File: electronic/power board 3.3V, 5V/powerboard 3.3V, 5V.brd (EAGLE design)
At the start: 46.7 x 31.7 mm, 10 parts, among them IC1_5V REG1117, IC2_3.3V REG1117, X1 GND, X3_5V 5V, X4_3.3V 3.3V, X5 IN

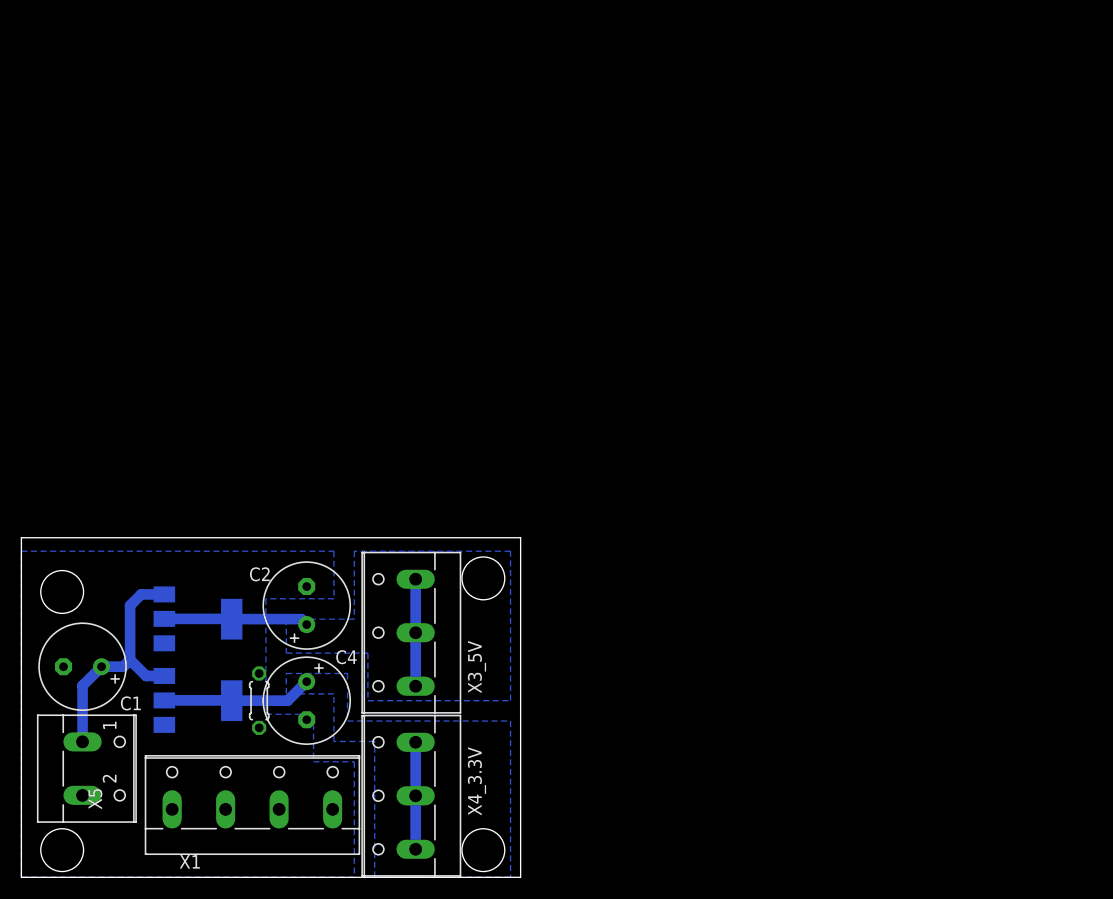
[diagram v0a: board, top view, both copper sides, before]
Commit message: moved schematics to the KiCad
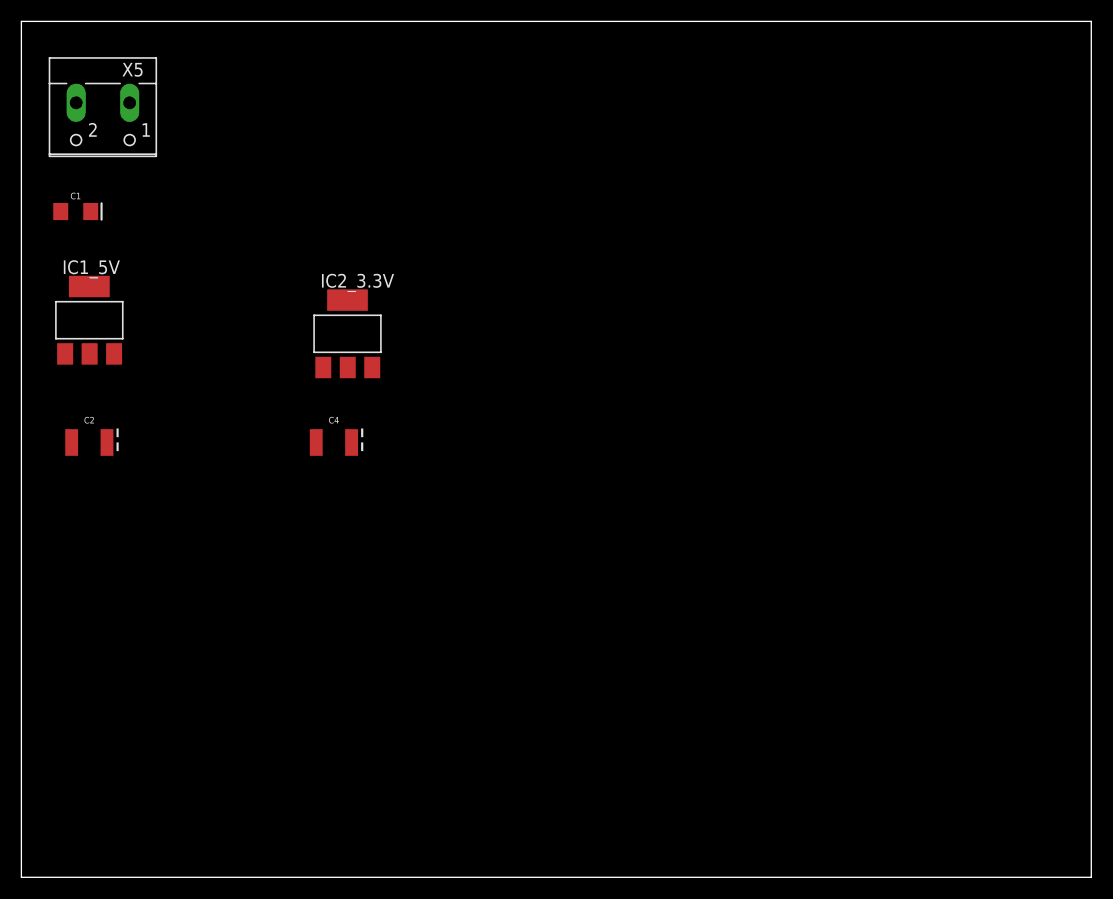
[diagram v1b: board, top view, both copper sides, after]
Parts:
- removed R1: 0, resistor:0204/5
- removed X1: GND, con-wago-500:W237-4
- removed X3_5V: 5V, con-wago-500:W237-103
- removed X4_3.3V: 3.3V, con-wago-500:W237-103
- C1: value 20uF -> 10uF; device resistor:E3,5-8 -> SparkFun-Capacitors:EIA3216
- C2, C4: value 100uF -> 22uF; device resistor:E3,5-8 -> SparkFun-Capacitors:EIA3528
- moved X5 61.0 mm to (7.62, 71.1), turned to 180 degrees
- moved C1 42.5 mm to (5.08, 62.2), turned to 0 degrees
- moved IC2_3.3V 37.0 mm to (30.5, 50.8), flipped to the top, turned to 0 degrees
- moved IC1_5V 29.7 mm to (6.35, 52.1), flipped to the top, turned to 0 degrees
- moved C2 25.4 mm to (6.35, 40.6), turned to 0 degrees
- moved C4 24.3 mm to (29.2, 40.6), turned to 0 degrees
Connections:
- net 3.3V: now also C4.A; no longer C4.+, X4_3.3V.1, X4_3.3V.2, X4_3.3V.3
- net 5V: now also C2.A, IC2_3.3V.3; no longer C2.+, X3_5V.1, X3_5V.2, X3_5V.3
- net GND: now also C2.C, C4.C; no longer C2.-, C4.-, R1.1, R1.2, X1.1, X1.2, X1.3, X1.4
- net VIN: no longer IC2_3.3V.3
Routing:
- net 3.3V: track 24.1 -> 0.00 mm
- net 5V: track 23.5 -> 0.00 mm
- net VIN: track 23.2 -> 0.00 mm
- removed copper zone on layer 16, net 3.3V
- removed copper zone on layer 16, net 5V
- removed copper zone on layer 16, net GND
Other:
- board size 46.7 x 31.7 mm -> 100 x 80 mm
